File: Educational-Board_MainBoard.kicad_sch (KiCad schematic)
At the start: 0 parts

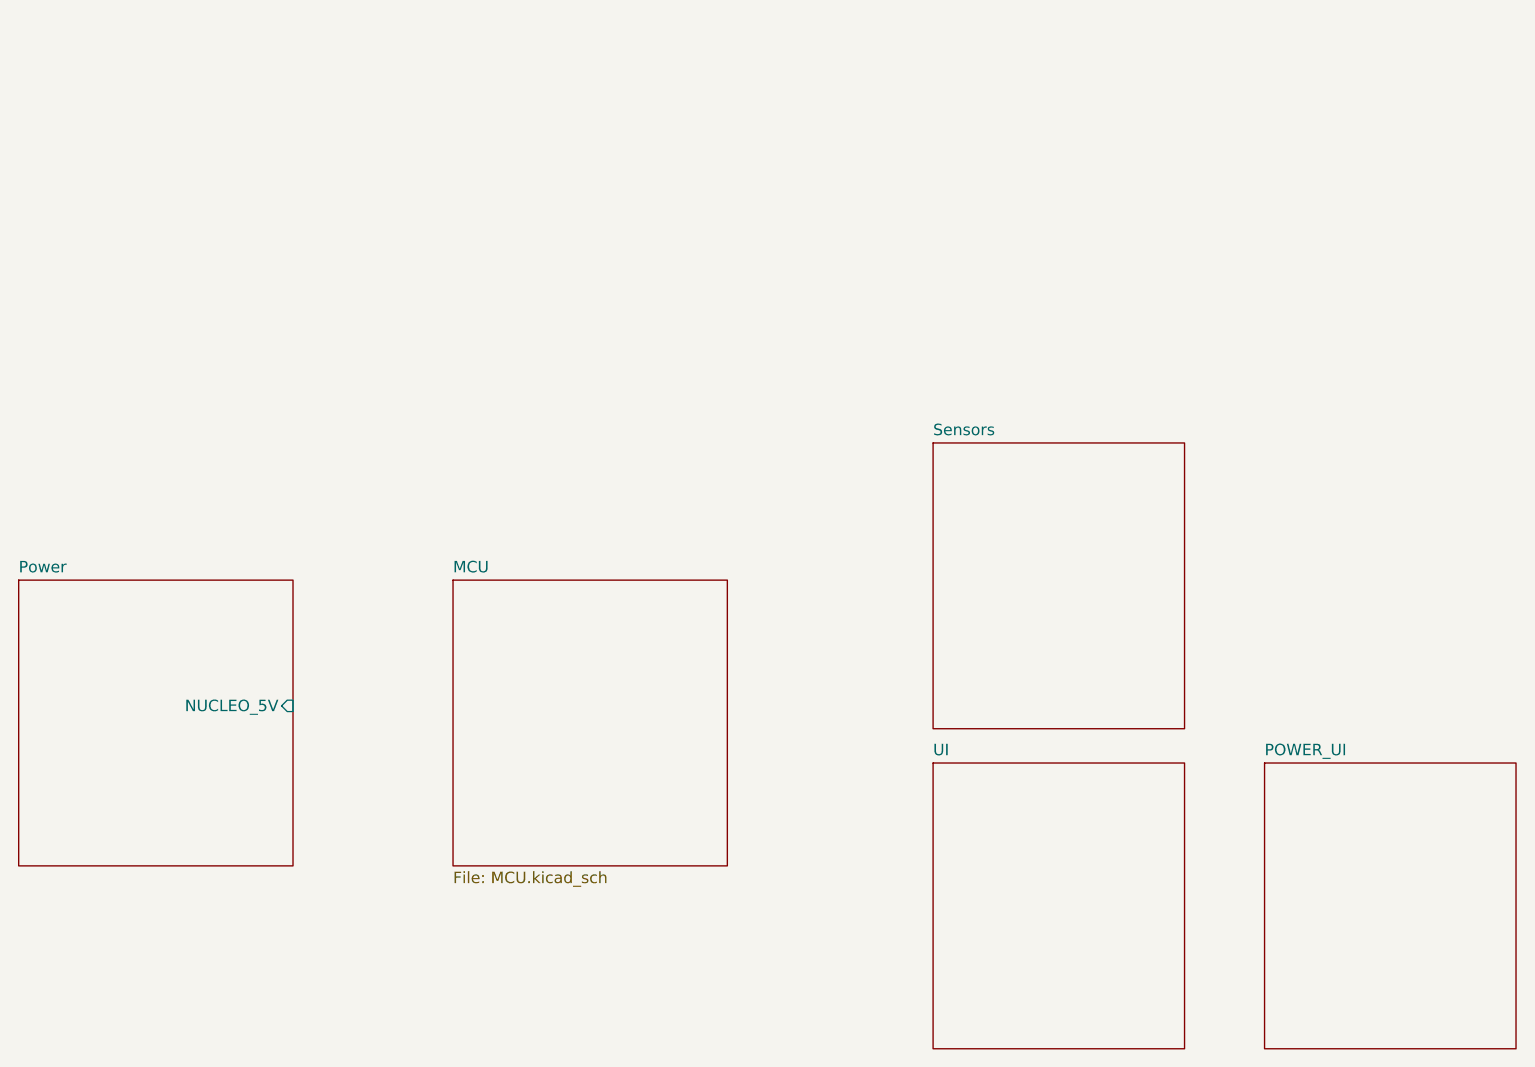
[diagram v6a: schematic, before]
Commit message: Added the hierarchical pins of the sheets and connected them, Fixes #7
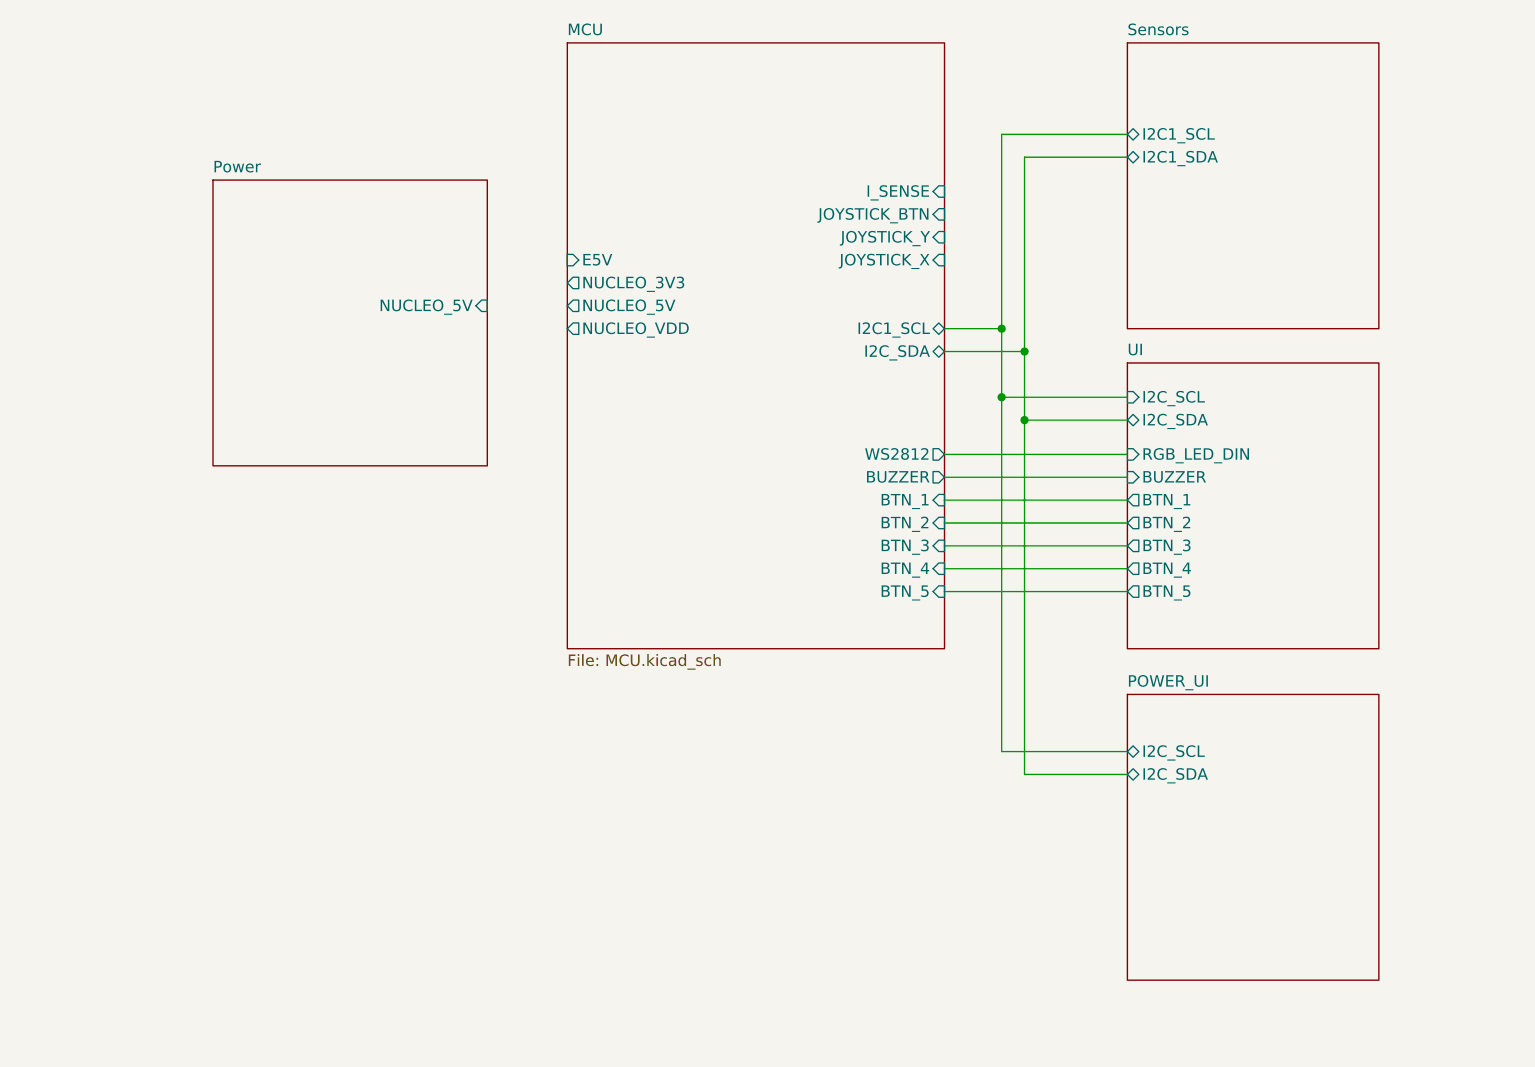
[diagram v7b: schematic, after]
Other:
- sheet MCU ports: added BTN_1, BTN_2, BTN_3, BTN_4, BTN_5, BUZZER, E5V, I2C1_SCL, I2C_SDA, I_SENSE, JOYSTICK_BTN, JOYSTICK_X, JOYSTICK_Y, NUCLEO_3V3, NUCLEO_5V, NUCLEO_VDD, WS2812; removed none
- sheet POWER_UI ports: added I2C_SCL, I2C_SDA; removed none
- sheet Sensors ports: added I2C1_SCL, I2C1_SDA; removed none
- sheet UI ports: added BTN_1, BTN_2, BTN_3, BTN_4, BTN_5, BUZZER, I2C_SCL, I2C_SDA, RGB_LED_DIN; removed none

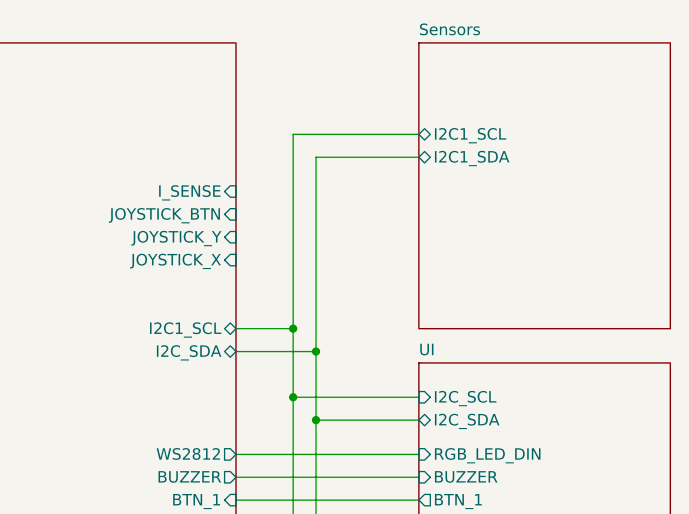
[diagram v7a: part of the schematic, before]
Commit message: Added hierarchical lablels to schematic
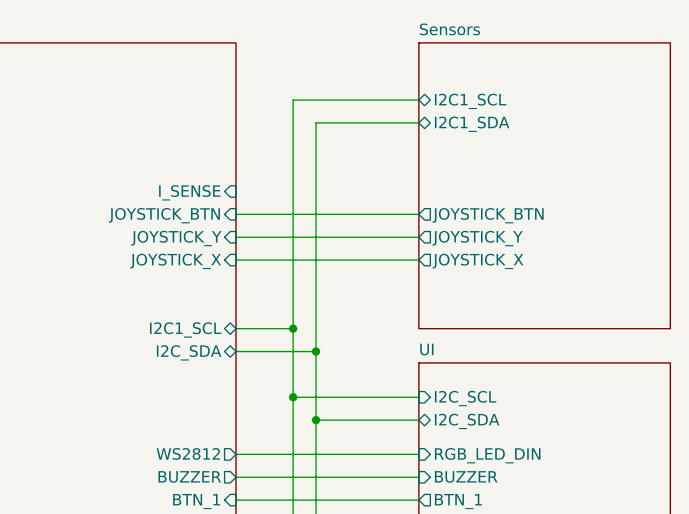
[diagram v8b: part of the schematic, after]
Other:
- sheet Sensors ports: added JOYSTICK_BTN, JOYSTICK_X, JOYSTICK_Y; removed none
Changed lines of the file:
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@@
+	(wire
+		(pts
+			(xy 153.67 53.34) (xy 173.99 53.34)
+		)
+		(stroke
+			(width 0)
+			(type default)
+		)
+	)
 	(wire
 		(pts
@@
 	(wire
 		(pts
-			(xy 162.56 44.45) (xy 162.56 66.04)
-		)
-		(stroke
-			(width 0)
-			(type default)
-		)
-	)
-	(wire
-		(pts
-			(xy 173.99 41.91) (xy 160.02 41.91)
+			(xy 162.56 40.64) (xy 162.56 66.04)
+		)
+		(stroke
+			(width 0)
+			(type default)
+		)
+	)
+	(wire
+		(pts
+			(xy 173.99 38.1) (xy 160.02 38.1)
 		)
 		(stroke
@@
 	(wire
 		(pts
-			(xy 160.02 41.91) (xy 160.02 63.5)
+			(xy 153.67 55.88) (xy 173.99 55.88)
+		)
+		(stroke
+			(width 0)
+			(type default)
+		)
+	)
+	(wire
+		(pts
+			(xy 160.02 38.1) (xy 160.02 63.5)
 		)
 		(stroke
@@
 	(wire
 		(pts
+			(xy 153.67 50.8) (xy 173.99 50.8)
+		)
+		(stroke
+			(width 0)
+			(type default)
+		)
+	)
+	(wire
+		(pts
 			(xy 153.67 87.63) (xy 173.99 87.63)
 		)
@@
 	(wire
 		(pts
-			(xy 173.99 44.45) (xy 162.56 44.45)
+			(xy 173.99 40.64) (xy 162.56 40.64)
 		)
 		(stroke
@@
 		)
 		(pin "I2C1_SCL" bidirectional
-			(at 173.99 41.91 180)
+			(at 173.99 38.1 180)
 			(effects
 				(font
@@
 		)
 		(pin "I2C1_SDA" bidirectional
-			(at 173.99 44.45 180)
-			(effects
-				(font
+			(at 173.99 40.64 180)
+			(effects
+				(font
+					(size 1.27 1.27)
+				)
+				(justify left)
+			)
+		)
+		(pin "JOYSTICK_BTN" output
+			(at 173.99 50.8 180)
+			(effects
+				(font
+					(size 1.27 1.27)
+				)
+				(justify left)
+			)
+		)
+		(pin "JOYSTICK_X" output
+			(at 173.99 55.88 180)
+			(effects
+				(font
+					(size 1.27 1.27)
+				)
+				(justify left)
+			)
+		)
+		(pin "JOYSTICK_Y" output
+			(at 173.99 53.34 180)
+			(effects
+				(font
